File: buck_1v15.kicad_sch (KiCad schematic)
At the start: 20 parts, among them U2 TPS564257DRLR

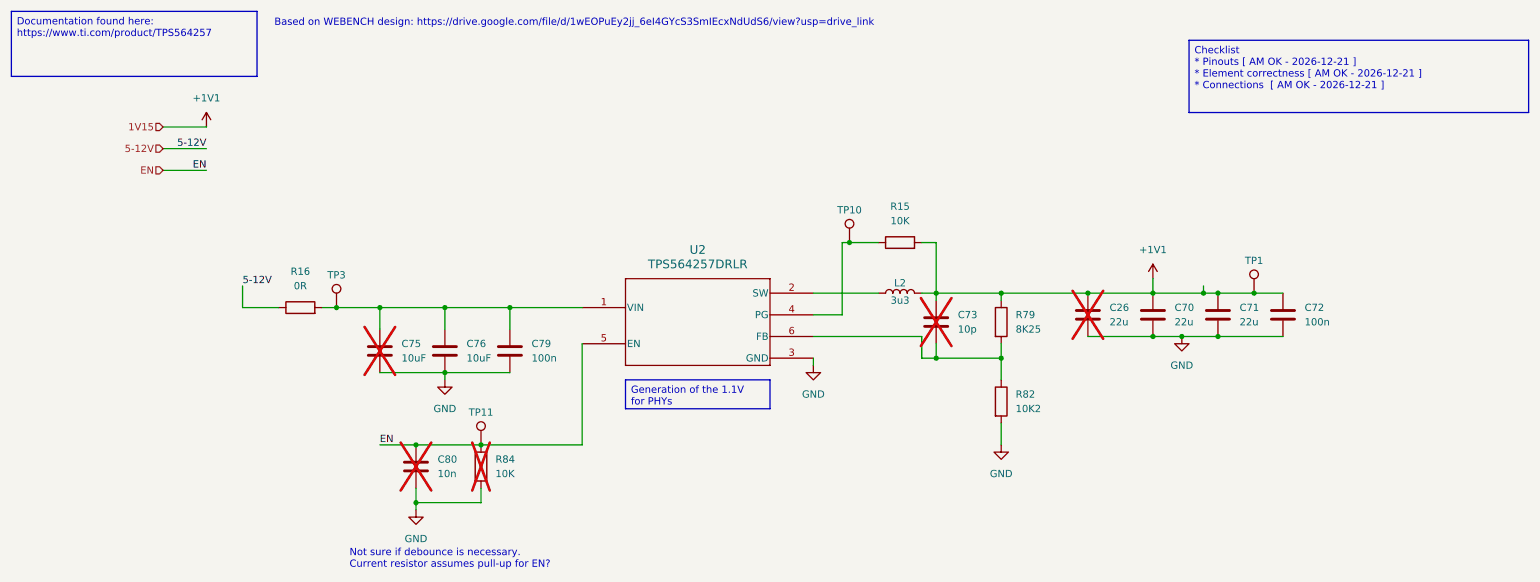
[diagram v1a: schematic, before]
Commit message: updates resistors and inductor symbol in 1V15 converter
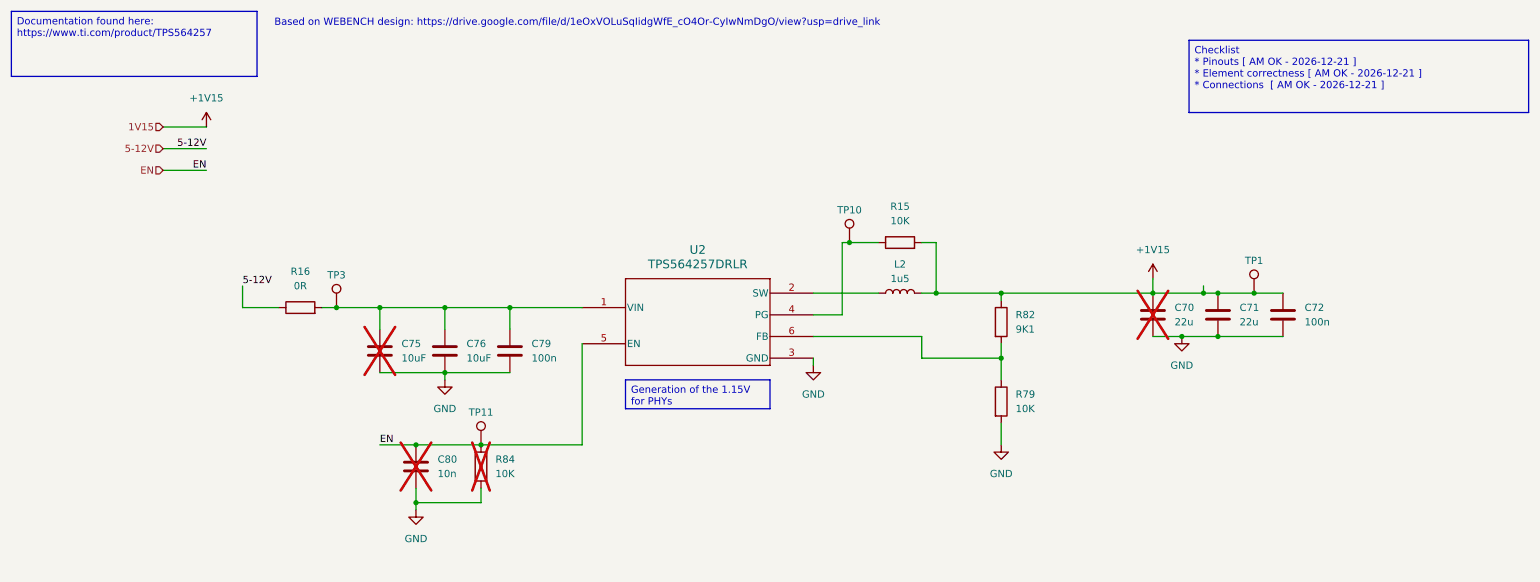
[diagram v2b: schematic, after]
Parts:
- removed C26: 22u, KL:C_0603, symbol KL_C:C_22u_10V_X5R_0603_20
- removed C73: 10p, Capacitor_SMD:C_0201_0603Metric, symbol KL_C:C_10p_25V_C0G_0603_5
- removed L2: 3u3, KL:L_3u3_EXLA1V0603, symbol KL_L:L_3u3_8A
- removed R79: 8K25, symbol KL_R:R_8K25_63mW_1_0402
- removed R82: 10K2, KL_Footprints:C_0603, symbol KL_R:R_10K2_100mW_1_0603
- added L2: 1u5, KL:L_1u5_SRP7050WA, symbol KL_L:L_1u5_19A_20pct_7L9x7W3
- added R79: 10K, KL_Footprints:C_0603, symbol KL_R:R_10K_100mW_5_0603
- added R82: 9K1, KL_Footprints:C_0603, symbol KL_R:R_9K1_100mW_1pct_0603
- C70: now not fitted; now left out of the parts list
- C75, C80, R84: now left out of the parts list
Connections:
- net GND: now also R79.2
- net at U2.6 (FB): now also R79.1, R82.2
- net at U2.2 (SW): now also L2.1
- net +1V1 renamed +1V15
- net +1V15: now also L2.2, R82.1
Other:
- note added: "Based on WEBENCH design: https://drive.google.com/file/d/1eOxVOLuSqIidgWfE_cO4Or-CyIwNmDgO/view?usp=drive_link"
- note removed: "Based on WEBENCH design: https://drive.google.com/file/d/1wEOPuEy2jj_6eI4GYcS3SmIEcxNdUdS6/view?usp=drive_link"
- note removed: "Not sure if debounce is necessary. Current resistor assumes pull-up for EN?"

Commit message: fixes ERC errors in DC/DC converters
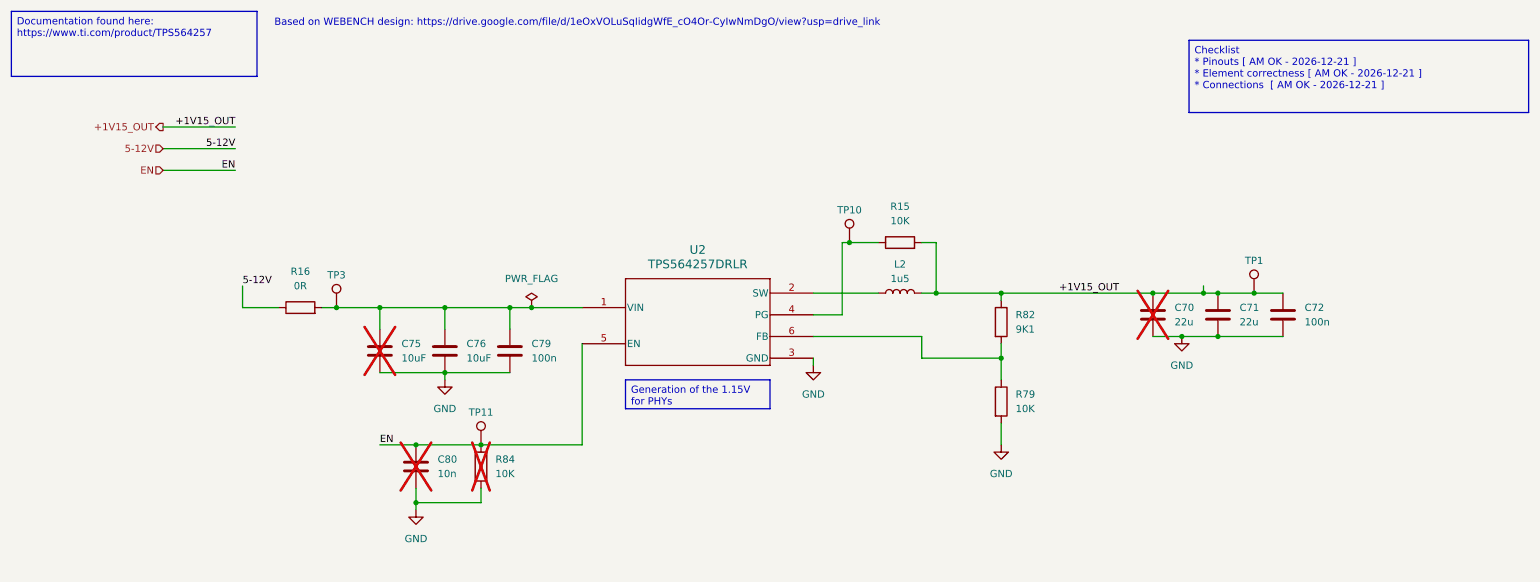
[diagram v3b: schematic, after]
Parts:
- C70: footprint KL:C_0603 -> KL_Footprints:C_0603; now in the parts list
- C71: footprint KL:C_0603 -> KL_Footprints:C_0603
- C72, C76, C79: footprint Capacitor_SMD:C_0201_0603Metric -> KL_Footprints:C_0603
- C75: footprint Capacitor_SMD:C_0201_0603Metric -> KL_Footprints:C_0603; now in the parts list
- L2: footprint KL:L_1u5_SRP7050WA -> KL_Footprints:SRP7050WA-1R5M
- R15, R79, R82: footprint KL_Footprints:C_0603 -> KL_Footprints:R_0603
- R84: footprint KL_Footprints:C_0603 -> KL_Footprints:R_0603; now in the parts list
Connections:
- net +1V15 renamed +1V15_OUT
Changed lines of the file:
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@@
 	)
 	(junction
+		(at 105.41 66.04)
+		(diameter 0)
+		(color 0 0 0 0)
+	)
+	(junction
 		(at 101.6 66.04)
 		(diameter 0)
@@
 	(wire
 		(pts
-			(xy 40.64 34.29) (xy 48.26 34.29)
+			(xy 40.64 34.29) (xy 53.34 34.29)
 		)
 		(stroke
@@
 	(wire
 		(pts
-			(xy 40.64 41.91) (xy 48.26 41.91)
+			(xy 40.64 41.91) (xy 53.34 41.91)
 		)
 		(stroke
@@
 	(wire
 		(pts
-			(xy 226.06 63.5) (xy 232.41 63.5)
+			(xy 105.41 66.04) (xy 114.3 66.04)
 		)
 		(stroke
@@
 	(wire
 		(pts
-			(xy 54.61 66.04) (xy 60.96 66.04)
+			(xy 226.06 63.5) (xy 232.41 63.5)
 		)
 		(stroke
@@
 	(wire
 		(pts
-			(xy 187.96 63.5) (xy 187.96 64.77)
+			(xy 54.61 66.04) (xy 60.96 66.04)
 		)
 		(stroke
@@
 	(wire
 		(pts
-			(xy 90.17 77.47) (xy 101.6 77.47)
+			(xy 187.96 63.5) (xy 187.96 64.77)
 		)
 		(stroke
@@
 	(wire
 		(pts
-			(xy 101.6 66.04) (xy 114.3 66.04)
+			(xy 90.17 77.47) (xy 101.6 77.47)
 		)
 		(stroke
@@
 	(wire
 		(pts
-			(xy 40.64 38.1) (xy 48.26 38.1)
+			(xy 101.6 66.04) (xy 105.41 66.04)
 		)
 		(stroke
@@
 	(wire
 		(pts
-			(xy 78.74 77.47) (xy 90.17 77.47)
+			(xy 40.64 38.1) (xy 53.34 38.1)
 		)
 		(stroke
@@
 	(wire
 		(pts
-			(xy 214.63 71.12) (xy 219.71 71.12)
+			(xy 78.74 77.47) (xy 90.17 77.47)
 		)
 		(stroke
@@
 	(wire
 		(pts
-			(xy 187.96 86.36) (xy 187.96 90.17)
+			(xy 214.63 71.12) (xy 219.71 71.12)
 		)
 		(stroke
@@
 	(wire
 		(pts
-			(xy 96.52 100.33) (xy 96.52 97.79)
+			(xy 187.96 86.36) (xy 187.96 90.17)
 		)
 		(stroke
@@
 	(wire
 		(pts
-			(xy 214.63 60.96) (xy 214.63 63.5)
+			(xy 96.52 100.33) (xy 96.52 97.79)
 		)
 		(stroke
@@
 	)
 	(label "5-12V"
-		(at 48.26 38.1 180)
+		(at 53.34 38.1 180)
 		(effects
 			(font
@@
 		)
 	)
+	(label "+1V15_OUT"
+		(at 198.12 63.5 0)
+		(effects
+			(font
+				(size 1.27 1.27)
+			)
+			(justify left bottom)
+		)
+	)
 	(label "EN"
-		(at 48.26 41.91 180)
+		(at 53.34 41.91 180)
 		(effects
 			(font
@@
 		)
 	)
-	(hierarchical_label "1V15"
-		(shape input)
+	(label "+1V15_OUT"
+		(at 53.34 34.29 180)
+		(effects
+			(font
+				(size 1.27 1.27)
+			)
+			(justify right bottom)
+		)
+	)
+	(hierarchical_label "+1V15_OUT"
+		(shape output)
 		(at 40.64 34.29 180)
 		(effects
@@
 			)
 		)
-		(property "Footprint" "KL_Footprints:C_0603"
+		(property "Footprint" "KL_Footprints:R_0603"
 			(at 186.182 68.58 90)
 			(effects
@@
 			)
 		)
-		(property "Footprint" "KL_Footprints:C_0603"
+		(property "Footprint" "KL_Footprints:R_0603"
 			(at 170.18 56.388 90)
 			(effects
@@
 			)
 		)
-		(property "Footprint" "Capacitor_SMD:C_0201_0603Metric"
+		(property "Footprint" "KL_Footprints:C_0603"
 			(at 238.4552 71.12 0)
 			(effects
@@
 			)
 		)
-		(property "Footprint" "Capacitor_SMD:C_0201_0603Metric"
+		(property "Footprint" "KL_Footprints:C_0603"
 			(at 91.1352 77.47 0)
 			(effects
@@
 		(unit 1)
 		(exclude_from_sim no)
-		(in_bom no)
+		(in_bom yes)
 		(on_board yes)
 		(dnp yes)
@@
 			)
 		)
-		(property "Footprint" "Capacitor_SMD:C_0201_0603Metric"
+		(property "Footprint" "KL_Footprints:C_0603"
 			(at 79.7052 77.47 0)
 			(effects
@@
 			)
 		)
-		(property "Footprint" "KL_Footprints:C_0603"
+		(property "Footprint" "KL_Footprints:R_0603"
 			(at 186.182 82.55 90)
 			(effects
@@
 		(unit 1)
 		(exclude_from_sim no)
-		(in_bom no)
+		(in_bom yes)
 		(on_board yes)
 		(dnp yes)
@@
 			)
 		)
-		(property "Footprint" "KL_Footprints:C_0603"
+		(property "Footprint" "KL_Footprints:R_0603"
 			(at 94.742 93.98 90)
 			(effects
@@
 			)
 		)
-		(property "Footprint" "KL:C_0603"
+		(property "Footprint" "KL_Footprints:C_0603"
 			(at 227.0252 71.12 0)
 			(effects
@@
 			)
 		)
-		(property "Footprint" "Capacitor_SMD:C_0201_0603Metric"
+		(property "Footprint" "KL_Footprints:C_0603"
 			(at 102.5652 77.47 0)
 			(effects
@@
 	)
 	(symbol
-		(lib_id "KL_TP:TestPoint")
-		(at 96.52 90.17 0)
+		(lib_id "KL_Flags:PWR_FLAG")
+		(at 105.41 66.04 0)
 		(unit 1)
 		(exclude_from_sim no)
@@
 		(dnp no)
 		(fields_autoplaced yes)
-		(property "Reference" "TP11"
-			(at 96.52 84.455 0)
-			(do_not_autoplace yes)
+		(property "Reference" "#FLG04"
+			(at 105.41 64.135 0)
 			(effects
 				(font
 					(size 1.27 1.27)
 				)
+				(hide yes)
 			)
 		)
-		(property "Value" "~"
-			(at 96.52 85.09 0)
+		(property "Value" "PWR_FLAG"
+			(at 105.41 60.96 0)
 			(effects
 				(font
 					(size 1.27 1.27)
 				)
-				(hide yes)
 			)
 		)
-		(property "Footprint" "Connector_PinHeader_2.54mm:PinHeader_1x01_P2.54mm_Vertical"
-			(at 101.6 90.17 0)
+		(property "Footprint" ""
+			(at 105.41 66.04 0)
 			(effects
 				(font
@@
 		)
 		(property "Datasheet" "~"
-			(at 101.6 90.17 0)
+			(at 105.41 66.04 0)
 			(effects
 				(font
@@
 			)
 		)
-		(property "Description" "test point"
-			(at 96.52 90.17 0)
+		(property "Description" "Special symbol for telling ERC where power comes from"
+			(at 105.41 66.04 0)
 			(effects
 				(font
@@
 		)
 		(instances
-			(project "switch"
-				(path "/cd936d40-9035-4ec8-bcf8-38758f995fb0/42c65065-b6e5-43b0-ae2c-34333f058269"
-					(reference "TP?")
-					(unit 1)
-				)
-			)
-			(project "shish-lan"
+			(project ""
 				(path "/d4536448-b109-4159-96e2-3dc21baf2d6e/0b7d9af9-83c1-43fa-a7a0-a33d0a00ea9c/42c65065-b6e5-43b0-ae2c-34333f058269"
-					(reference "TP11")
+					(reference "#FLG04")
 					(unit 1)
 				)
@@
 	)
 	(symbol
-		(lib_id "KL_SYM_LOCAL:+1V1")
-		(at 214.63 60.96 0)
+		(lib_id "KL_TP:TestPoint")
+		(at 96.52 90.17 0)
 		(unit 1)
 		(exclude_from_sim no)
@@
 		(dnp no)
 		(fields_autoplaced yes)
-		(property "Reference" "#PWR10"
-			(at 214.63 64.77 0)
+		(property "Reference" "TP11"
+			(at 96.52 84.455 0)
+			(do_not_autoplace yes)
 			(effects
 				(font
 					(size 1.27 1.27)
 				)
-				(hide yes)
 			)
 		)
-		(property "Value" "+1V15"
-			(at 214.63 55.88 0)
+		(property "Value" "~"
+			(at 96.52 85.09 0)
 			(effects
 				(font
 					(size 1.27 1.27)
 				)
+				(hide yes)
 			)
 		)
-		(property "Footprint" ""
-			(at 214.63 60.96 0)
+		(property "Footprint" "Connector_PinHeader_2.54mm:PinHeader_1x01_P2.54mm_Vertical"
+			(at 101.6 90.17 0)
 			(effects
 				(font
@@
 			)
 		)
-		(property "Datasheet" ""
-			(at 214.63 60.96 0)
+		(property "Datasheet" "~"
+			(at 101.6 90.17 0)
 			(effects
 				(font
@@
 			)
 		)
-		(property "Description" "Power symbol creates a global label with name \"+1V1\""
-			(at 214.63 60.96 0)
+		(property "Description" "test point"
+			(at 96.52 90.17 0)
 			(effects
 				(font
@@
 			(project "switch"
 				(path "/cd936d40-9035-4ec8-bcf8-38758f995fb0/42c65065-b6e5-43b0-ae2c-34333f058269"
-					(reference "#PWR?")
+					(reference "TP?")
 					(unit 1)
 				)
 			)
-			(project ""
+			(project "shish-lan"
 				(path "/d4536448-b109-4159-96e2-3dc21baf2d6e/0b7d9af9-83c1-43fa-a7a0-a33d0a00ea9c/42c65065-b6e5-43b0-ae2c-34333f058269"
-					(reference "#PWR10")
+					(reference "TP11")
 					(unit 1)
 				)
@@
 		(unit 1)
 		(exclude_from_sim no)
-		(in_bom no)
+		(in_bom yes)
 		(on_board yes)
 		(dnp yes)
@@
 			)
 		)
-		(property "Footprint" "KL:C_0603"
+		(property "Footprint" "KL_Footprints:C_0603"
 			(at 215.5952 71.12 0)
 			(effects
@@
 			)
 		)
-		(property "Footprint" "KL:L_1u5_SRP7050WA"
+		(property "Footprint" "KL_Footprints:SRP7050WA-1R5M"
 			(at 166.37 56.388 0)
 			(effects
@@
 			)
 		)
-		(property "Datasheet" ""
-			(at 166.37 55.88 0)
+		(property "Datasheet" "https://www.bourns.com/docs/Product-Datasheets/SRP7050WA.pdf"
+			(at 166.37 63.5 0)
 			(effects
 				(font
@@
 					(unit 1)
 				)
-			)
-		)
-	)
-	(symbol
-		(lib_id "KL_SYM_LOCAL:+1V1")
-		(at 48.26 34.29 0)
-		(unit 1)
-		(exclude_from_sim no)
-		(in_bom yes)
-		(on_board yes)
-		(dnp no)
-		(fields_autoplaced yes)
-		(property "Reference" "#PWR22"
-			(at 48.26 38.1 0)
-			(effects
-				(font
-					(size 1.27 1.27)
-				)
-				(hide yes)
-			)
-		)
-		(property "Value" "+1V15"
-			(at 48.26 29.21 0)
-			(effects
-				(font
-					(size 1.27 1.27)
-				)
-			)
-		)
-		(property "Footprint" ""
-			(at 48.26 34.29 0)
-			(effects
-				(font
-					(size 1.27 1.27)
-				)
-				(hide yes)
-			)
-		)
-		(property "Datasheet" ""
-			(at 48.26 34.29 0)
-			(effects
-				(font
-					(size 1.27 1.27)
-				)
-				(hide yes)
-			)
-		)
-		(property "Description" "Power symbol creates a global label with name \"+1V1\""
-			(at 48.26 34.29 0)
-			(effects
-				(font
-					(size 1.27 1.27)
-				)
-				(hide yes)
-			)
-		)
-		(pin "1"
-		)
-		(instances
-			(project "switch"
-				(path "/cd936d40-9035-4ec8-bcf8-38758f995fb0/42c65065-b6e5-43b0-ae2c-34333f058269"
-					(reference "#PWR?")
-					(unit 1)
-				)
-			)
-			(project ""
-				(path "/d4536448-b109-4159-96e2-3dc21baf2d6e/0b7d9af9-83c1-43fa-a7a0-a33d0a00ea9c/42c65065-b6e5-43b0-ae2c-34333f058269"
-					(reference "#PWR22")
-					(unit 1)
-				)

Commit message: updates components from my library misconfiguration. Refs: #1
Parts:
- C80: footprint Capacitor_SMD:C_0201_0603Metric -> KL_Footprints:C_0603; now in the parts list
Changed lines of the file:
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@@
 		(unit 1)
 		(exclude_from_sim no)
-		(in_bom no)
+		(in_bom yes)
 		(on_board yes)
 		(dnp yes)
@@
 			)
 		)
-		(property "Footprint" "Capacitor_SMD:C_0201_0603Metric"
+		(property "Footprint" "KL_Footprints:C_0603"
 			(at 86.0552 97.79 0)
 			(effects

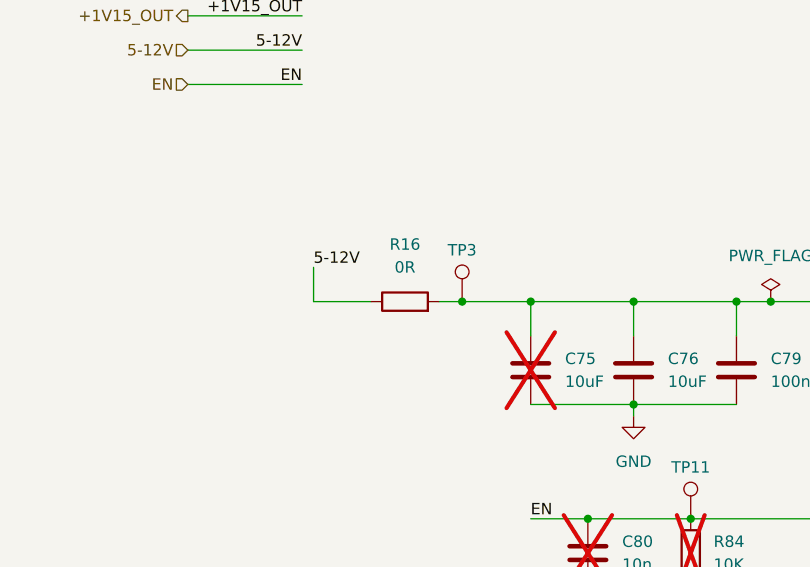
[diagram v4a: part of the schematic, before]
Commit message: removes unused busses, adds cheaper 0R resistor, clean up to fix ERC errors. Refs: #1
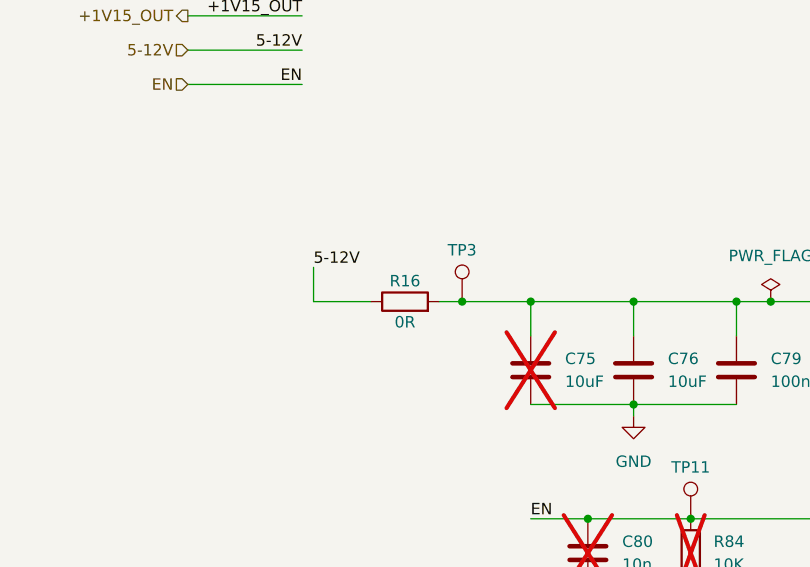
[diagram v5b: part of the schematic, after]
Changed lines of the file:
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@@
 		(on_board yes)
 		(dnp no)
-		(fields_autoplaced yes)
 		(property "Reference" "R16"
-			(at 64.77 59.69 90)
+			(at 64.77 63.754 90)
 			(effects
 				(font
@@
 		)
 		(property "Value" "0R"
-			(at 64.77 62.23 90)
+			(at 64.77 68.326 90)
 			(effects
 				(font
